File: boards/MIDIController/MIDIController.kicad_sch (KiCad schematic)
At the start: 1 part

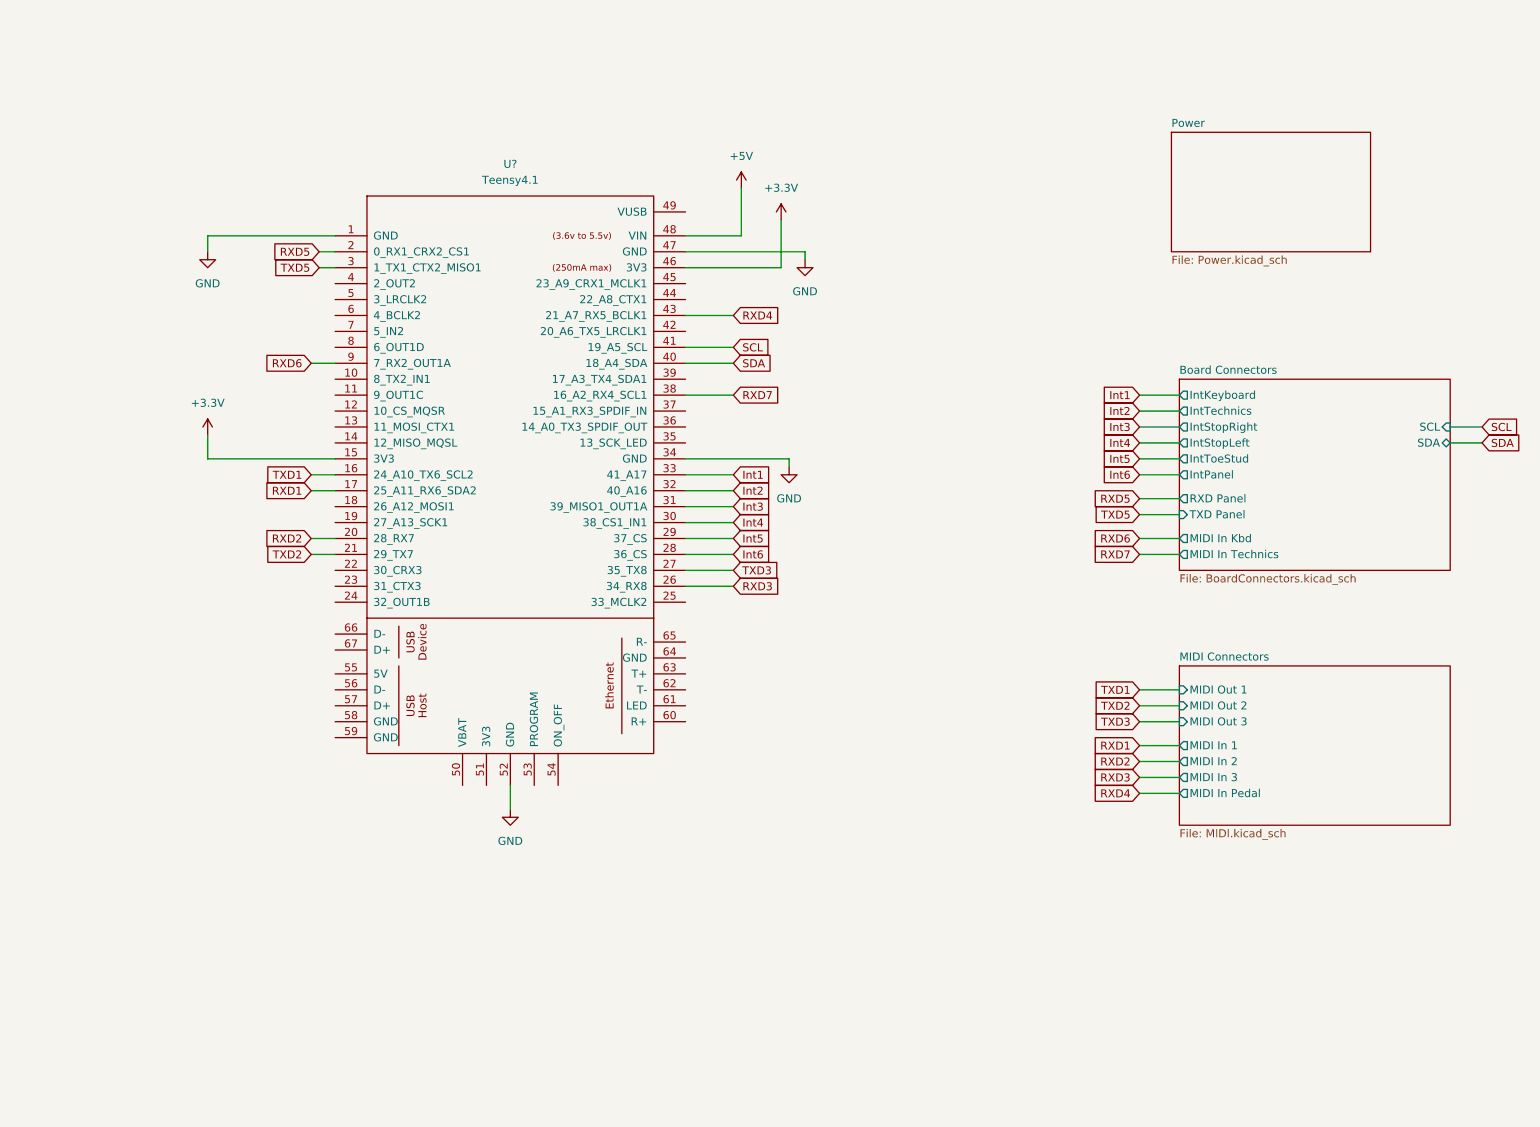
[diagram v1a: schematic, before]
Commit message: Created new signals drawings
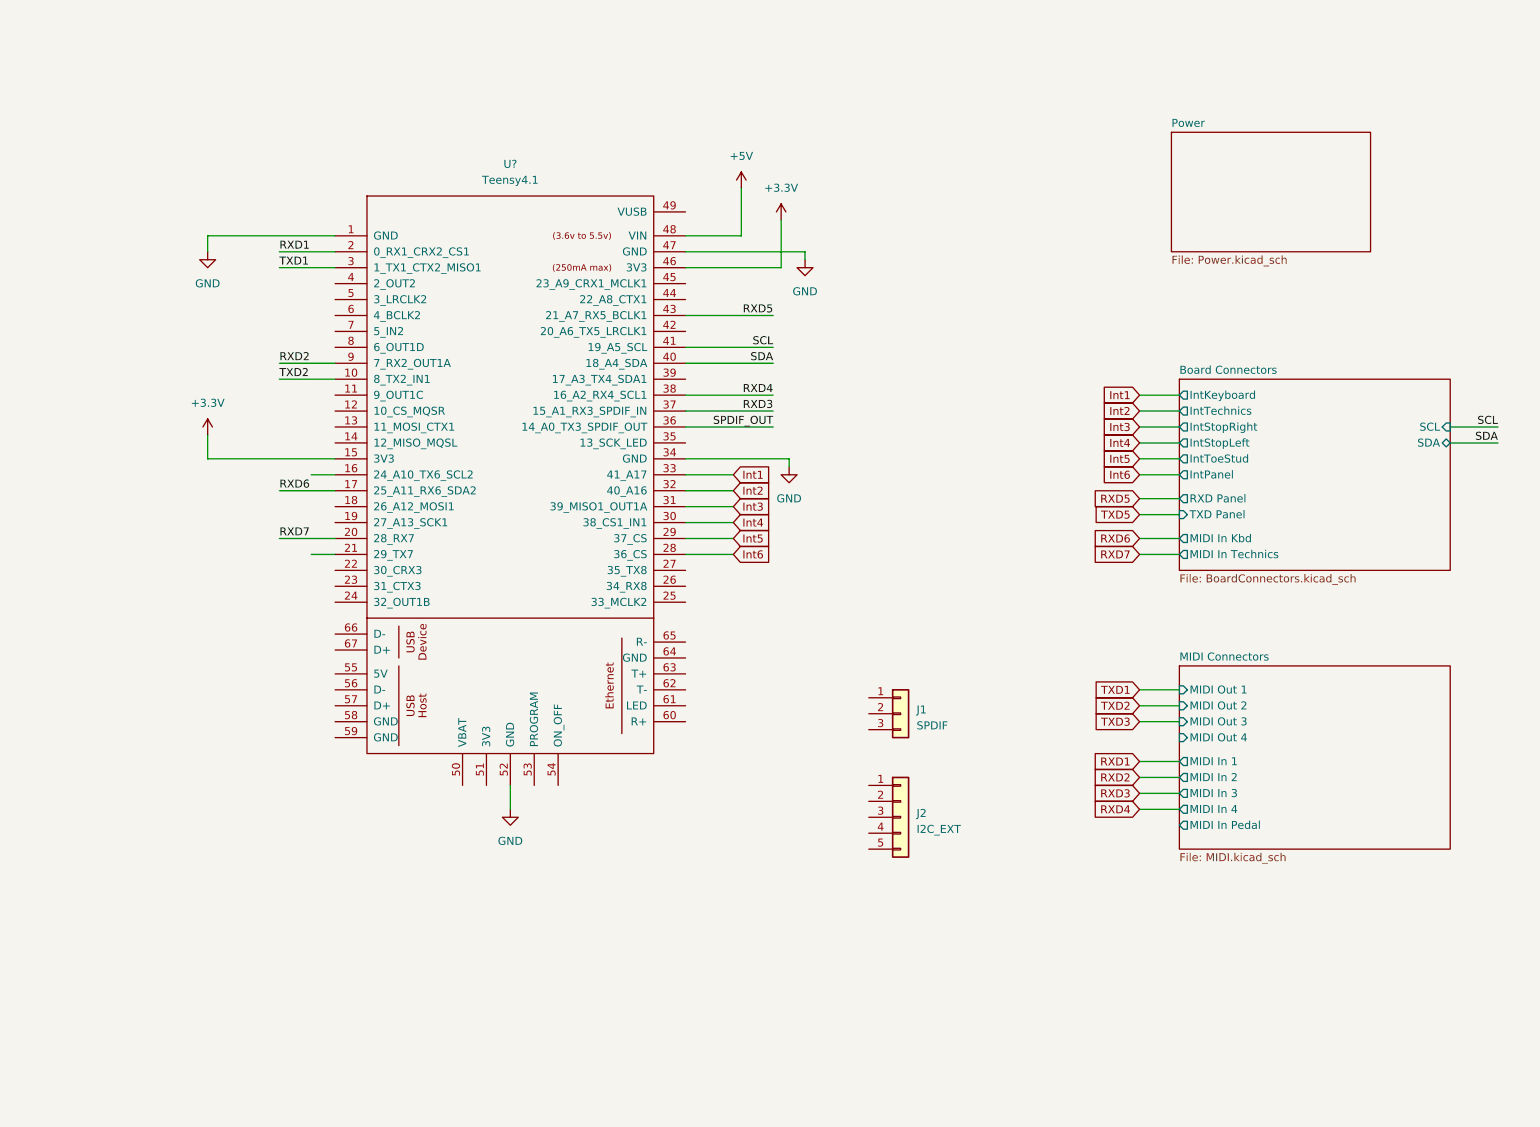
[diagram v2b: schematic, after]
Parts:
- added J1: SPDIF, symbol Connector_Generic:Conn_01x03
- added J2: I2C_EXT, symbol Connector_Generic:Conn_01x05
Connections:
- net RXD1: now also U?.2 (0_RX1_CRX2_CS1); no longer U?.17 (25_A11_RX6_SDA2)
- net RXD2: now also U?.9 (7_RX2_OUT1A); no longer U?.20 (28_RX7)
- net RXD3: now also U?.37 (15_A1_RX3_SPDIF_IN); no longer U?.26 (34_RX8)
- net RXD4: now also U?.38 (16_A2_RX4_SCL1); no longer U?.43 (21_A7_RX5_BCLK1)
- net RXD5: now also U?.43 (21_A7_RX5_BCLK1); no longer U?.2 (0_RX1_CRX2_CS1)
- net RXD6: now also U?.17 (25_A11_RX6_SDA2); no longer U?.9 (7_RX2_OUT1A)
- net RXD7: now also U?.20 (28_RX7); no longer U?.38 (16_A2_RX4_SCL1)
- net TXD1: now also U?.3 (1_TX1_CTX2_MISO1); no longer U?.16 (24_A10_TX6_SCL2)
- net TXD2: now also U?.10 (8_TX2_IN1); no longer U?.21 (29_TX7)
- net TXD3: no longer U?.27 (35_TX8)
- net TXD5: no longer U?.3 (1_TX1_CTX2_MISO1)
- net SPDIF_OUT: now reaches U?.36 (14_A0_TX3_SPDIF_OUT)
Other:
- sheet MIDI Connectors ports: added MIDI In 4, MIDI Out 4; removed none

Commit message: Added Audio frontpanel, added more MIDI ports to controller
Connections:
- net TXD5: now also U?.42 (20_A6_TX5_LRCLK1)
- net TXD6: now reaches U?.16 (24_A10_TX6_SCL2)
- net TXD7: now reaches U?.21 (29_TX7)
- net RXD8: now reaches U?.26 (34_RX8)
- net TXD4: now reaches U?.39 (17_A3_TX4_SDA1)

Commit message: Cleanup of PCB sizes and mounthole positions. Moved MIDI connectors to separate board.
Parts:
- gave numbers to parts that had none: 1
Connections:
- net Int1 renamed INT1
- net Int2 renamed INT2
- net Int3 renamed INT3
- net Int4 renamed INT4
- net Int5 renamed INT5
- net Int6 renamed INT6

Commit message: Added Optocoupler and RS232 converter to UART board lines.
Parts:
- removed J1: SPDIF, symbol Connector_Generic:Conn_01x03
- removed J2: I2C_EXT, symbol Connector_Generic:Conn_01x05
- added BT1: Battery_Cell, symbol Device:Battery_Cell
- added C1: 100nF, symbol Device:C
- added C2: C_Polarized, symbol Device:C_Polarized
- added H1, H2, H3, H4: MountingHole, MountingHole:MountingHole_3.2mm_M3, symbol Mechanical:MountingHole
- added J1: RJ45_Abracon_ARJP11A-MASA-B-A-EMU2, Connector_RJ:RJ45_Abracon_ARJP11A-MA_Horizontal, symbol Connector:RJ45_Abracon_ARJP11A-MASA-B-A-EMU2
- added J4: USB_A, Connector_USB:USB_A_Molex_67643_Horizontal, symbol Connector:USB_A
- added J5: I2S Data, symbol Connector_Generic:Conn_01x06
- added J6: I2S Pwr, symbol Connector_Generic:Conn_01x06
- U1: footprint (none) -> Teensy:Teensy41
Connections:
- net +3.3V: now also J6.2 (Pin_2)
- net +5V: now also C1.1, C2.1, J6.1 (Pin_1)
- net GND: now also BT1.2 (-), C1.2, C2.2, J5.6 (Pin_6), J6.5 (Pin_5), J6.6 (Pin_6)
- net SCL: now also J6.3 (Pin_3)
- net SDA: now also J6.4 (Pin_4)
- net I2S_MCLK2: now reaches U1.25 (33_MCLK2)
- net I2S_MCLK2: now also J5.1 (Pin_1)
- net I2S_OUT2: now reaches U1.4 (2_OUT2)
- net I2S_OUT2: now also J5.2 (Pin_2)
- net I2S_LRCLK2: now reaches U1.5 (3_LRCLK2)
- net I2S_LRCLK2: now also J5.3 (Pin_3)
- net at U1.50 (VBAT): now also BT1.1 (+)
- net at U1.55 (5V): now also J4.1 (VBUS)
- net at U1.56 (D-): now also J4.2 (D-)
- net at U1.57 (D+): now also J4.3 (D+)
- net at U1.58 (GND): now also U1.59 (GND), J4.4 (GND)
- net I2S_BCLK2: now reaches U1.6 (4_BCLK2)
- net I2S_BCLK2: now also J5.4 (Pin_4)
- net I2S_IN2: now reaches U1.7 (5_IN2)
- net I2S_IN2: now also J5.5 (Pin_5)
- no-connect marks 0 -> 4
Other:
- removed sheet MIDI Connectors
- removed sheet Power
- sheet Board Connectors ports: added MIDI In 1, MIDI In 2, MIDI In 3, MIDI In 4, MIDI In Pedal, MIDI Out 1, MIDI Out 2, MIDI Out 3, MIDI Out 4; removed none

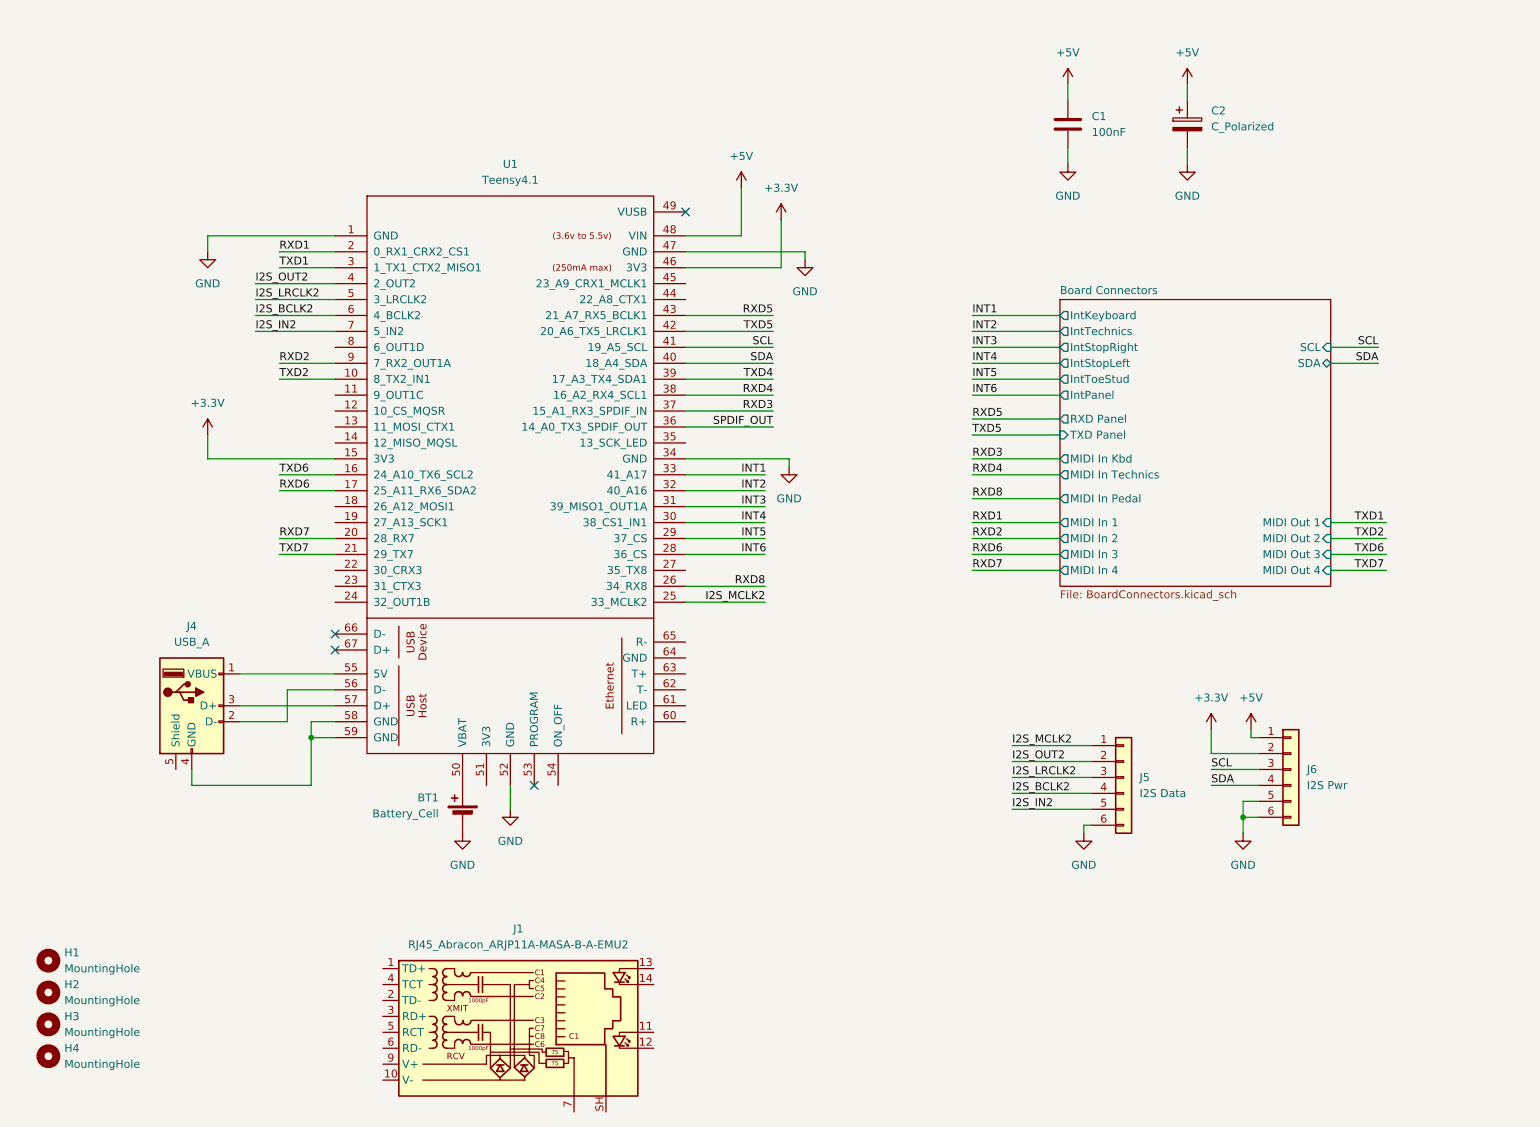
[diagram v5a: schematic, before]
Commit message: Finished connectors on MIDIController board, fixed 3.3V IO voltage levels
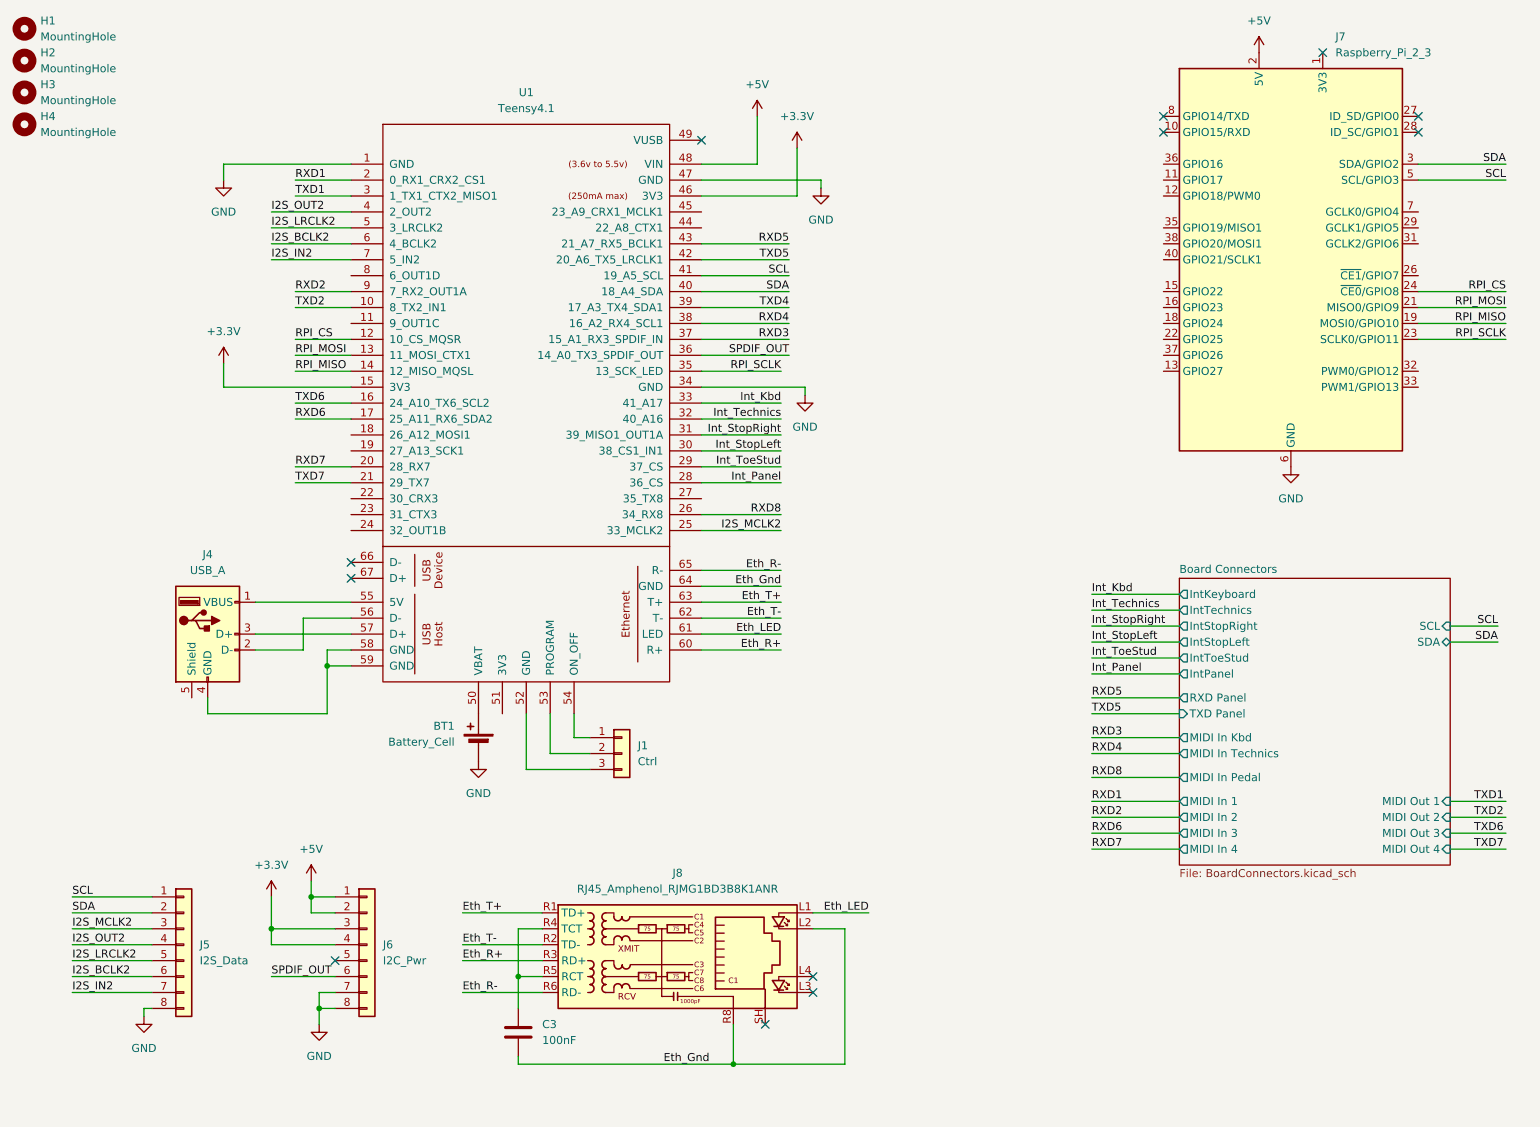
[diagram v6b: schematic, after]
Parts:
- removed C1: 100nF, symbol Device:C
- removed C2: C_Polarized, symbol Device:C_Polarized
- removed J1: RJ45_Abracon_ARJP11A-MASA-B-A-EMU2, Connector_RJ:RJ45_Abracon_ARJP11A-MA_Horizontal, symbol Connector:RJ45_Abracon_ARJP11A-MASA-B-A-EMU2
- removed J5: I2S Data, symbol Connector_Generic:Conn_01x06
- removed J6: I2S Pwr, symbol Connector_Generic:Conn_01x06
- added C3: 100nF, symbol Device:C
- added J1: Ctrl, symbol Connector_Generic:Conn_01x03
- added J5: I2S_Data, symbol Connector_Generic:Conn_01x08
- added J6: I2C_Pwr, symbol Connector_Generic:Conn_01x08
- added J7: Raspberry_Pi_2_3, Connector_PinHeader_2.54mm:PinHeader_2x20_P2.54mm_Vertical, symbol Connector:Raspberry_Pi_2_3
- added J8: RJ45_Amphenol_RJMG1BD3B8K1ANR, Connector_RJ:RJ45_Amphenol_RJMG1BD3B8K1ANR, symbol Connector:RJ45_Amphenol_RJMG1BD3B8K1ANR
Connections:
- net +3.3V: now also J6.3 (Pin_3), J6.4 (Pin_4)
- net +5V: now also J6.1 (Pin_1), J6.2 (Pin_2), J7.2 (5V), J7.4 (5V)
- net GND: now also J5.8 (Pin_8), J6.7 (Pin_7), J6.8 (Pin_8), J7.14 (GND), J7.20 (GND), J7.25 (GND), J7.30 (GND), J7.34 (GND), J7.39 (GND), J7.6 (GND), J7.9 (GND); no longer U1.52 (GND)
- net I2S_BCLK2: now also J5.6 (Pin_6)
- net I2S_IN2: now also J5.7 (Pin_7)
- net I2S_LRCLK2: now also J5.5 (Pin_5)
- net I2S_MCLK2: now also J5.3 (Pin_3)
- net I2S_OUT2: now also J5.4 (Pin_4)
- net SCL: now also J5.1 (Pin_1), J7.5 (SCL/GPIO3)
- net SDA: now also J5.2 (Pin_2), J7.3 (SDA/GPIO2)
- net SPDIF_OUT: now also J6.6 (Pin_6)
- net RPI_CS: now reaches U1.12 (10_CS_MQSR)
- net RPI_CS: now also J7.24 (~{CE0}/GPIO8)
- net RPI_MOSI: now reaches U1.13 (11_MOSI_CTX1)
- net RPI_MOSI: now also J7.21 (MISO0/GPIO9)
- net RPI_MISO: now reaches U1.14 (12_MISO_MQSL)
- net RPI_MISO: now also J7.19 (MOSI0/GPIO10)
- net RPI_SCLK: now reaches U1.35 (13_SCK_LED)
- net RPI_SCLK: now also J7.23 (SCLK0/GPIO11)
- net at U1.53 (PROGRAM): now also J1.2 (Pin_2)
- net at U1.54 (ON_OFF): now also J1.1 (Pin_1)
- net Eth_R+: now reaches U1.60 (R+)
- net Eth_R+: now also J8.R3 (RD+)
- net Eth_LED: now reaches U1.61 (LED)
- net Eth_LED: now also J8.L1
- net Eth_T-: now reaches U1.62 (T-)
- net Eth_T-: now also J8.R2 (TD-)
- net Eth_T+: now reaches U1.63 (T+)
- net Eth_T+: now also J8.R1 (TD+)
- net Eth_Gnd: now reaches U1.64 (GND)
- net Eth_Gnd: now also C3.2, J8.L2, J8.R8
- net Eth_R-: now reaches U1.65 (R-)
- net Eth_R-: now also J8.R6 (RD-)
- net INT1 renamed Int_Kbd
- net INT2 renamed Int_Technics
- net INT3 renamed Int_StopRight
- net INT4 renamed Int_StopLeft
- net INT5 renamed Int_ToeStud
- net INT6 renamed Int_Panel
- new net: C3.1, J8.R4 (TCT), J8.R5 (RCT)
- new net: J7.1 (3V3), J7.17 (3V3)
- new net: J1.3 (Pin_3), U1.52 (GND)
- no-connect marks 4 -> 12
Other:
- moved on the sheet: BT1, H1, H2, H3, H4, J4, U1

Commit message: Updated MidiController PCB footprints
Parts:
- C3: footprint (none) -> Capacitor_THT:C_Disc_D4.3mm_W1.9mm_P5.00mm
- J1: footprint (none) -> Connector_PinHeader_2.54mm:PinHeader_1x03_P2.54mm_Vertical
- J5, J6: footprint (none) -> Connector_PinHeader_2.54mm:PinHeader_1x08_P2.54mm_Vertical
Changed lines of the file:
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@@
 			)
 		)
-		(property "Footprint" ""
+		(property "Footprint" "Connector_PinHeader_2.54mm:PinHeader_1x08_P2.54mm_Vertical"
 			(at 72.39 165.1 0)
 			(effects
@@
 			)
 		)
-		(property "Footprint" ""
+		(property "Footprint" "Connector_PinHeader_2.54mm:PinHeader_1x08_P2.54mm_Vertical"
 			(at 43.18 165.1 0)
 			(effects
@@
 			)
 		)
-		(property "Footprint" ""
+		(property "Footprint" "Capacitor_THT:C_Disc_D4.3mm_W1.9mm_P5.00mm"
 			(at 97.4852 182.88 0)
 			(effects
@@
 			)
 		)
-		(property "Footprint" ""
+		(property "Footprint" "Connector_PinHeader_2.54mm:PinHeader_1x03_P2.54mm_Vertical"
 			(at 113.03 134.62 0)
 			(effects
